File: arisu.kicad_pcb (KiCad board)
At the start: 2 copper layers, 339.1 x 118.7 mm, 176 parts, among them J1 USB_B_Micro, SW1 SW_Push, SW10 SW_Push, SW11 SW_Push, SW12 SW_Push, SW13 SW_Push, SW14 SW_Push, SW15 SW_Push, SW16 SW_Push, SW17 SW_Push, SW18 SW_Push, SW19 SW_Push, SW2 SW_Push, SW20 SW_Push, SW21 SW_Push, SW22 SW_Push, SW23 SW_Push, SW24 SW_Push, SW25 SW_Push, SW26 SW_Push, SW27 SW_Push, SW28 SW_Push, SW29 SW_Push, SW3 SW_Push, SW30 SW_Push, SW31 SW_Push, SW32 SW_Push, SW33 SW_Push, SW34 SW_Push, SW35 SW_Push, SW36 SW_Push, SW37 SW_Push, SW38 SW_Push, SW39 SW_Push, SW4 SW_Push, SW40 SW_Push, SW41 SW_Push, SW42 SW_Push, SW43 SW_Push, SW44 SW_Push, SW45 SW_Push, SW46 SW_Push, SW47 SW_Push, SW48 SW_Push, SW49 SW_Push, SW5 SW_Push, SW50 SW_Push, SW51 SW_Push, SW52 SW_Push, SW53 SW_Push, SW54 SW_Push, SW55 SW_Push, SW56 SW_Push, SW57 SW_Push, SW58 SW_Push, SW59 SW_Push, SW6 SW_Push, SW60 SW_Push, SW61 SW_Push, SW62 SW_Push, SW63 SW_Push, SW64 SW_Push, SW65 SW_Push, SW66 SW_Push, SW67 SW_Push, SW7 SW_Push, SW8 SW_Push, SW9 SW_Push, U1 USBLC6-2SC6, U2 ATmega32U4-AU, Y1 Crystal_GND24

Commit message: change micro usb to mini usb
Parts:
- removed J1: USB_B_Micro, Connectors_USB:USB_Micro-B_Molex-105017-0001
- added REF**: USB_Mini-B_Lumberg_2486_01_Horizontal, Connector_USB:USB_Mini-B_Lumberg_2486_01_Horizontal, B.Cu at (175.5, 28.4)
- moved C3 5.34 mm to (188.0, 27.9)
- moved C4 4.89 mm to (185.4, 27.9)
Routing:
- net GND: track 71.6 -> 59.5 mm
- net Net-(C4-Pad1): track 8.19 -> 14.2 mm
- net /col11: track 224.6 -> 230.6 mm
- net Net-(J1-Pad2): track 45.1 -> 40.4 mm
- net Net-(J1-Pad3): track 47.8 -> 51.2 mm
- net /col6: track 97.9 -> 96.8 mm
- net VCC: track 205.4 -> 204.7 mm
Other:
- board text added: "Fate Design Rev 1.1"
- board text removed: "Fate Design Rev 1.0"

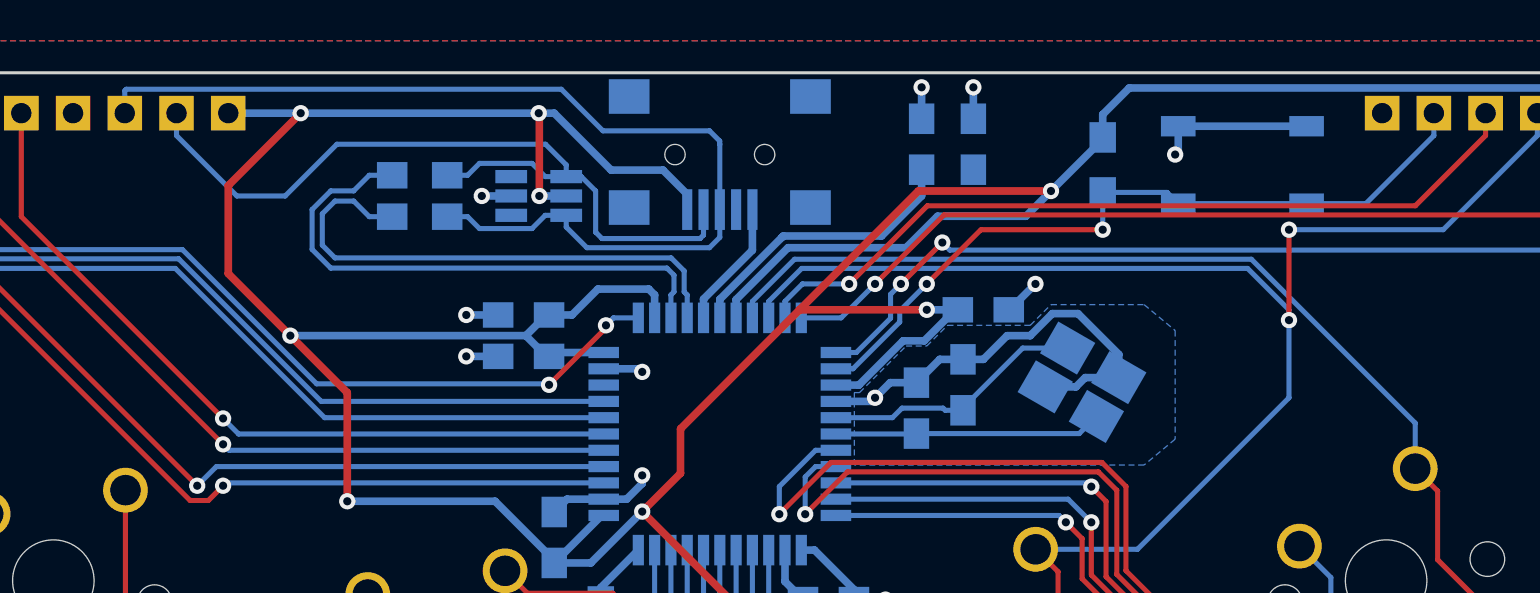
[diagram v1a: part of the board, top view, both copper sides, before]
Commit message: v2.0 with usb c
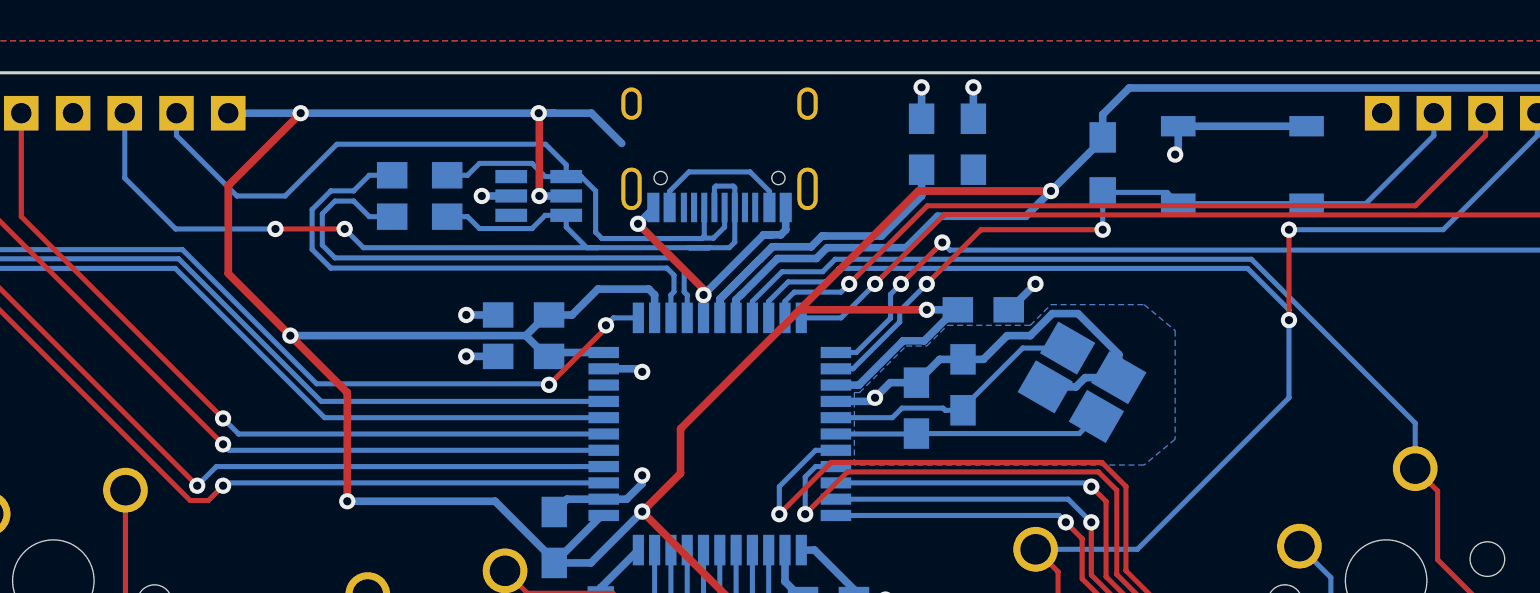
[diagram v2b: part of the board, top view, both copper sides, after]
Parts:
- removed the REF** at (175.5, 28.4)
- added REF**: USB_C_Receptacle_HRO_TYPE-C-31-M-12, Connector_USB:USB_C_Receptacle_HRO_TYPE-C-31-M-12, B.Cu at (175.5, 27.0)
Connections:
- D+ pad 1: Net-(J1-Pad3) -> D+
- D- pad 1: Net-(J1-Pad2) -> D-
- R1 pad 2: Net-(J1-Pad3) -> D+
- R2 pad 2: Net-(J1-Pad2) -> D-
- U1 pad 4: Net-(J1-Pad2) -> D-
- U1 pad 6: Net-(J1-Pad3) -> D+
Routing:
- net Net-(J1-Pad3): track 51.2 -> 0.00 mm
- net D+: track 26.2 -> 76.5 mm, vias 0 -> 2
- net D-: track 27.0 -> 69.9 mm
- net Net-(J1-Pad2): track 40.4 -> 0.00 mm
- net GND: track 59.5 -> 67.1 mm, vias 12 -> 14
- net (no net): track 0.00 -> 7.28 mm
- net Net-(C4-Pad1): track 14.2 -> 19.0 mm
- net VCC: track 204.7 -> 201.4 mm
